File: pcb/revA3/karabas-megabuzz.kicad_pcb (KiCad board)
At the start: 4 copper layers, 92.2 x 44 mm, 173 parts, among them J1 FPGA JTAG, J2 Conn_02x31_Row_Letter_First, J3 uSD card, J4 PJ307, J5 Conn_01x04, J6 PRG, J7 NMI, T1 TestPoint1, T2 TestPoint2, T3 TestPoint, T4 TestPoint, T5 TestPoint, T6 TestPoint, T7 TestPoint, U1 XC6SLX25-FTG256, U10 YMF262-M, U11 SAM2695, U12 PCM5102A, U13 PCM1808PWR, U14 CY62167EV30LL, U15 1117-3.3, U16 1117-3.3, U17 1117-1.2, U18 APS6404L-3SQRx-SN, U19 74AHCT1G125DB, U2 W25Q128JVS, U20 AS6C1008-xxST, U21 24LC08, U22 VS1053, U23 XC6206P182MR, U3 74AHCT1G125DB, U4 74AHCT1G125DB, U5 SN74CB3T3245PW, U6 SN74CB3T3245PW, U7 SN74CB3T3245PW, U8 SN74CB3T3245PW, U9 SN74LV1T34DBV, X1 50 MHz

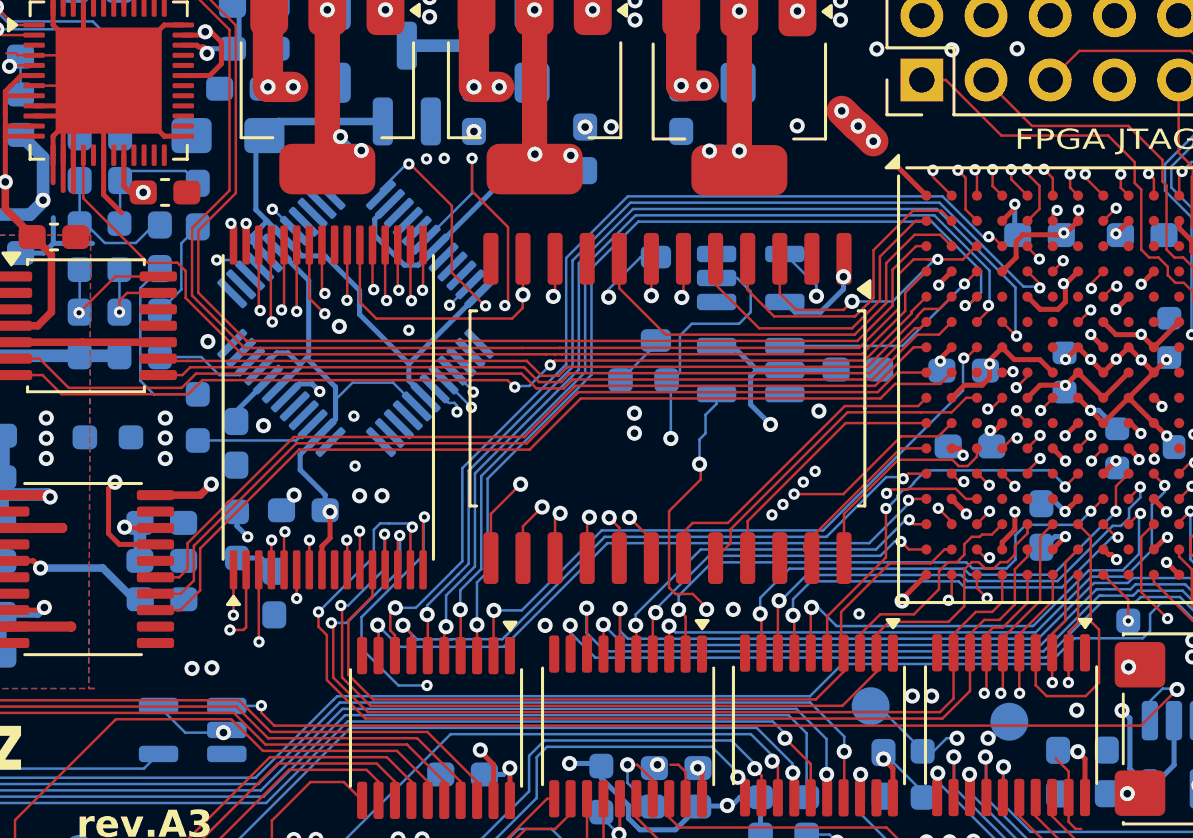
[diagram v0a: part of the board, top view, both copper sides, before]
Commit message: Updated revA3 with required additional pullups
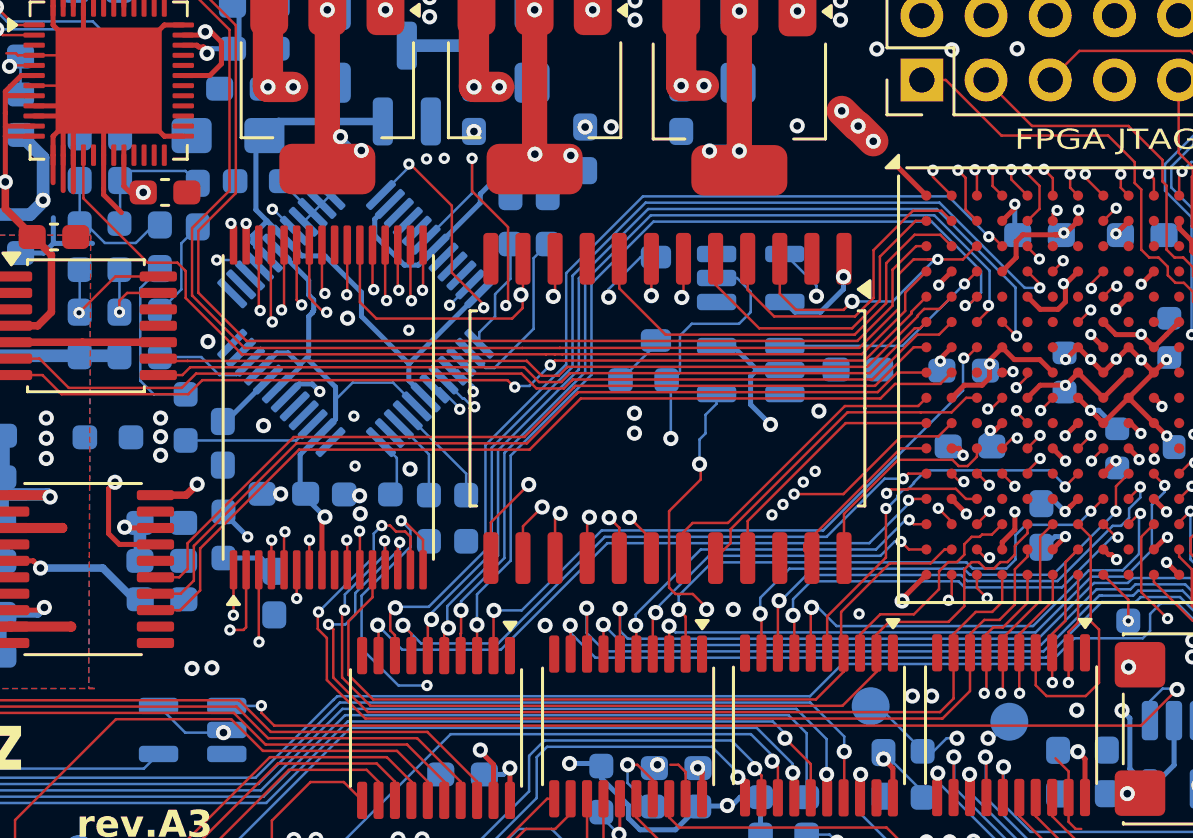
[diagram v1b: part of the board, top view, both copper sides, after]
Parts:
- added R16: 10k, Resistor_SMD:R_0603_1608Metric_Pad0.98x0.95mm_HandSolder, B.Cu at (142.5, 101.8)
- added R17: 100k, Resistor_SMD:R_0603_1608Metric_Pad0.98x0.95mm_HandSolder, B.Cu at (139.2, 113.6)
- added R18: 100k, Resistor_SMD:R_0603_1608Metric_Pad0.98x0.95mm_HandSolder, B.Cu at (137.8, 113.6)
- added R19: 100k, Resistor_SMD:R_0603_1608Metric_Pad0.98x0.95mm_HandSolder, B.Cu at (135.3, 112.6)
- added R29: 100k, Resistor_SMD:R_0603_1608Metric_Pad0.98x0.95mm_HandSolder, B.Cu at (141.0, 101.8)
- added R56: 100k, Resistor_SMD:R_0603_1608Metric_Pad0.98x0.95mm_HandSolder, B.Cu at (131.0, 100.2)
- moved C58 1.01 mm to (132.0, 112.6)
- moved C64 0.53 mm to (129.6, 110.6)
- moved R28 0.53 mm to (129.6, 114.2)
- moved R25 0.48 mm to (128.1, 109.6)
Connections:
- U22 pad 10: unconnected-(U22-GPIO3/SDATA-Pad10) -> Net-(U22-GPIO2/DCLK)
- U22 pad 11: unconnected-(U22-GPIO6/I2S_SCLK-Pad11) -> Net-(U22-GPIO2/DCLK)
- U22 pad 12: unconnected-(U22-GPIO7/I2S_SDATA-Pad12) -> Net-(U22-GPIO2/DCLK)
- U22 pad 25: unconnected-(U22-GPIO5/I2S_MCLK-Pad25) -> Net-(U22-GPIO5/I2S_MCLK)
- U22 pad 26: unconnected-(U22-RX-Pad26) -> Net-(U22-RX)
- U22 pad 33: unconnected-(U22-GPIO0-Pad33) -> Net-(U22-GPIO0)
- U22 pad 34: unconnected-(U22-GPIO1-Pad34) -> Net-(U22-GPIO1)
- U22 pad 36: unconnected-(U22-GPIO4/I2S_LROUT-Pad36) -> Net-(U22-GPIO4/I2S_LROUT)
- U22 pad 9: unconnected-(U22-GPIO2/DCLK-Pad9) -> Net-(U22-GPIO2/DCLK)
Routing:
- net Net-(U22-RX): track 0.00 -> 6.98 mm
- net Net-(U22-GPIO5/I2S_MCLK): track 0.00 -> 4.46 mm
- net Net-(U22-GPIO0): track 0.00 -> 4.12 mm
- net Net-(U22-GPIO1): track 0.00 -> 3.30 mm
- net Net-(U22-GPIO2/DCLK): track 0.00 -> 3.27 mm
- net Net-(U22-GPIO4/I2S_LROUT): track 0.00 -> 2.44 mm
- net +3V3: track 225.9 -> 227.6 mm
- net xA7: track 40.9 -> 40.2 mm
- net xD1: track 71.6 -> 72.2 mm
- net GND: vias 123 -> 124
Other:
- board text removed: "Special thanks to Caasper911"
